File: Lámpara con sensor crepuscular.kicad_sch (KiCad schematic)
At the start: 8 parts, among them J1 NA COM NC, J2 +12V GND, K1 G5LE-1, Q1 BC547

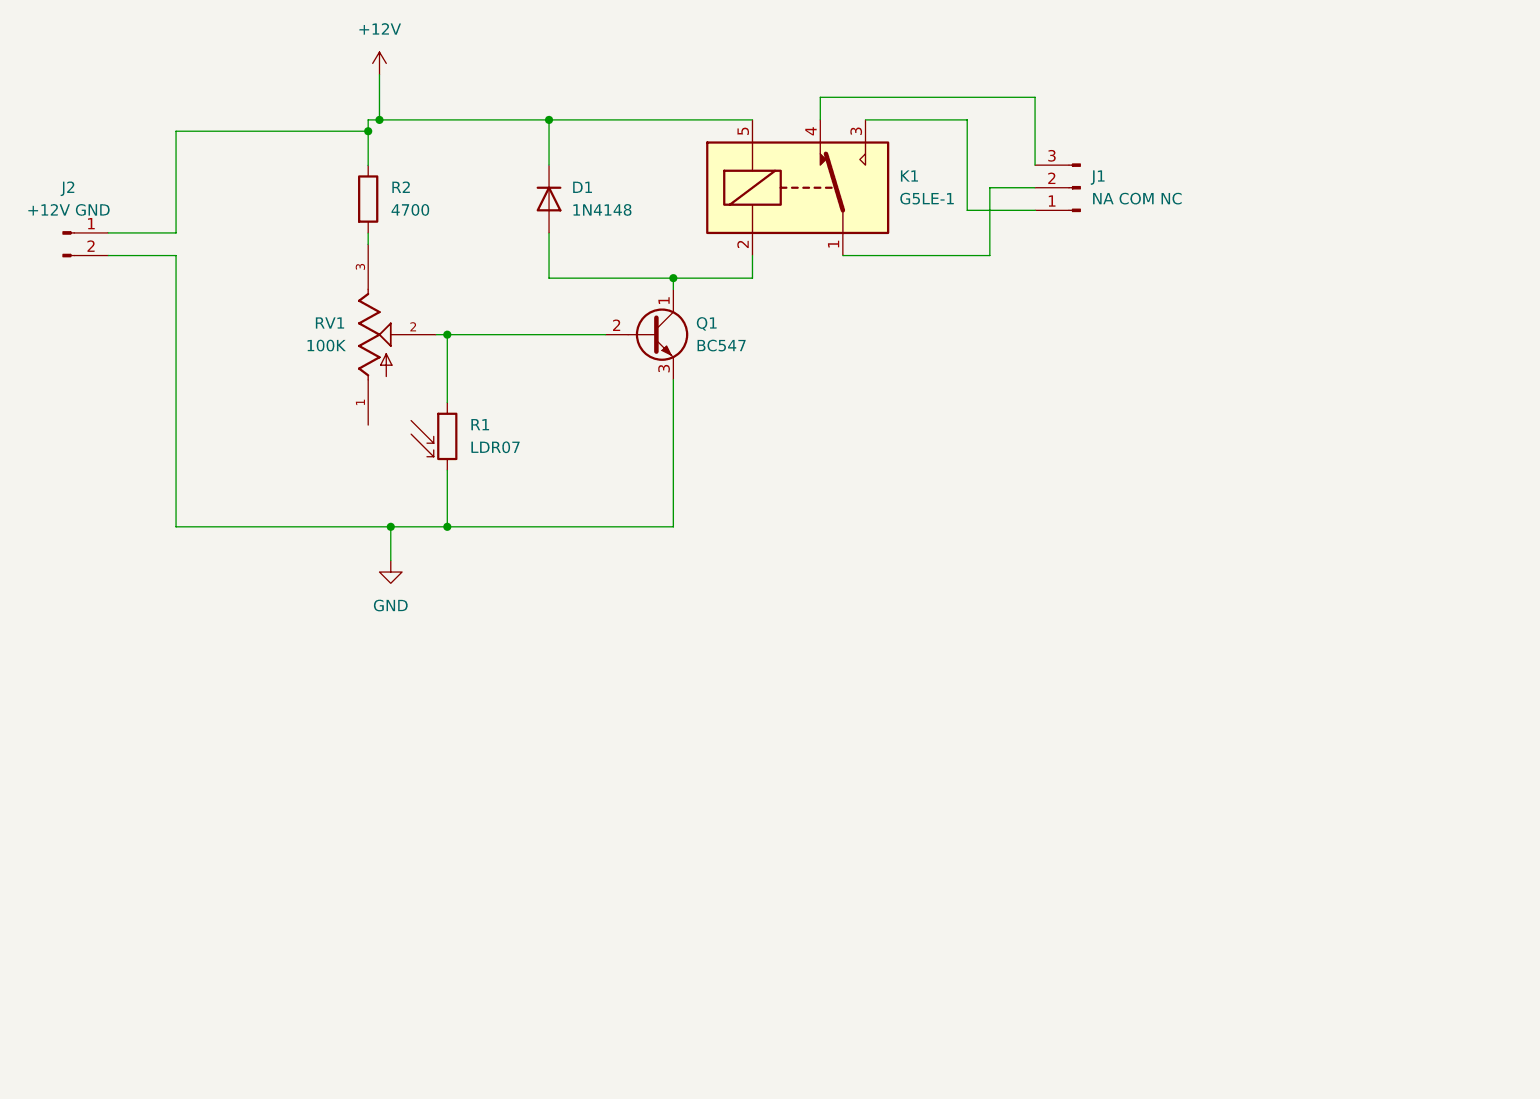
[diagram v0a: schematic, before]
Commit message: Añadir carpetas para guardar los archivos gerber, POS y BOM organizados por carpetas, hacer un README correspondiente al proyecto, colocar imagenes y videos referentes al proyecto como visualización en 3D, Esquemático y simulación del circuito
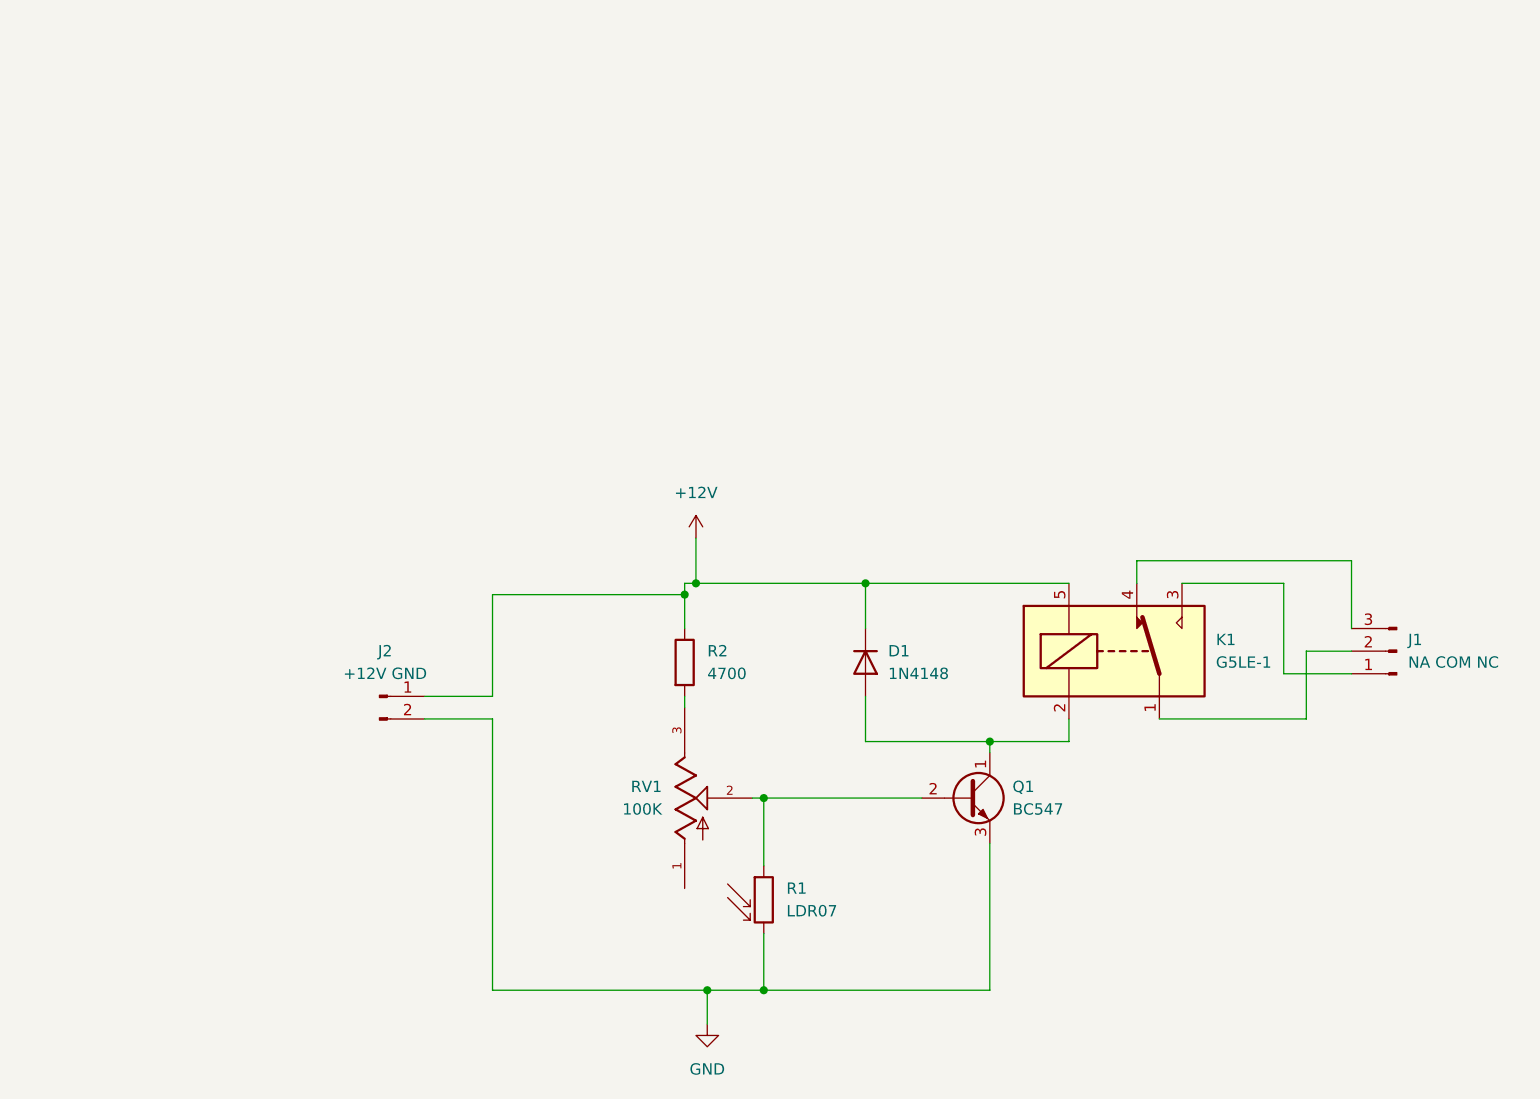
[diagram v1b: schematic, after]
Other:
- company: (none) -> Mexatrónica
- title: (none) -> Lámpara con sensor crepuscular
- moved on the sheet: D1, J1, J2, K1, Q1, R1, R2, RV1
